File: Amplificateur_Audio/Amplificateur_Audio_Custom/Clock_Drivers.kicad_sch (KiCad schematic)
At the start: 59 parts, among them J301 Conn_02x10_Odd_Even, Q301 NMOS, Q302 NMOS, U301 74LVC1G125, U302 74LVC1G125, U303 74LVC1G125, U304 74LVC1G125, U305 74LVC1G125, U306 74LVC1G125, U307 74LVC1G125, U308 74LVC1G125, U309 74LVC1G125, U310 74LVC1G125

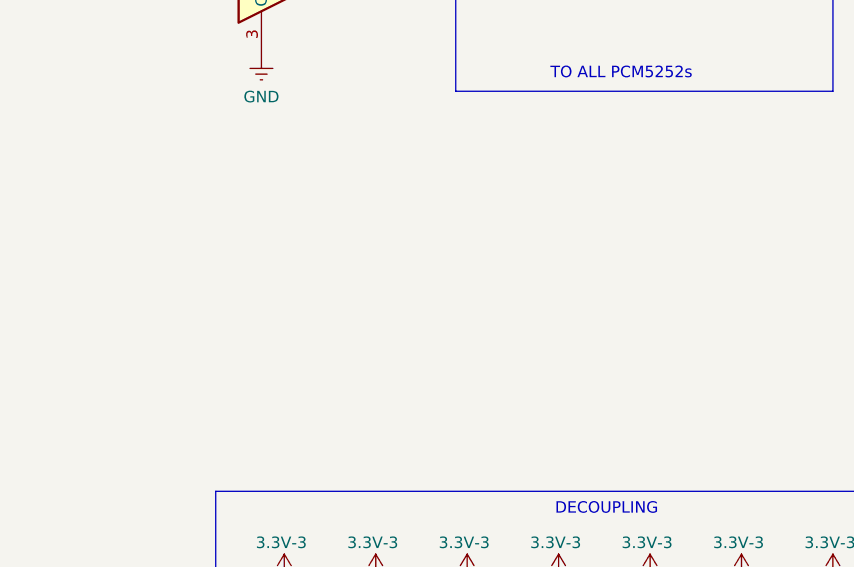
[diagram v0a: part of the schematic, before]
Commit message: Ajout de l'assignation des compostants et des empreintes jusqu'à la page 6
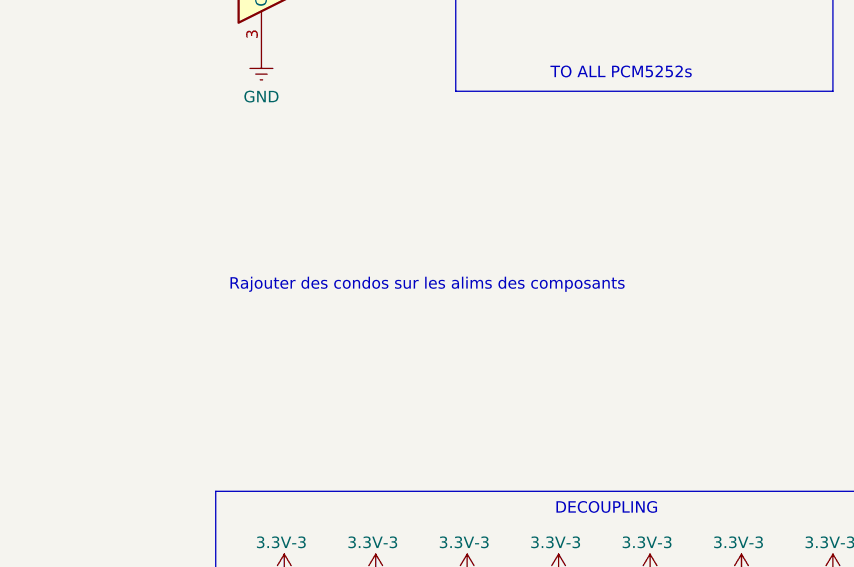
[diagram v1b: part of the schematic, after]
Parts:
- C301, C302, C303, C304, C305, C306, C307, C308: footprint (none) -> Capacitor_SMD:C_0402_1005Metric_Pad0.74x0.62mm_HandSolder
- D301, D302: footprint (none) -> LED_SMD:LED_0805_2012Metric_Pad1.15x1.40mm_HandSolder
- J301: footprint (none) -> Connector_IDC:IDC-Header_2x10_P2.54mm_Vertical_SMD
- Q301, Q302: footprint (none) -> Package_TO_SOT_SMD:SOT-23
- R301, R302, R303, R304, R305, R306, R307, R308, R309, R310, R311, R312, R313, R314, R315, R316, R317, R318: footprint (none) -> Resistor_SMD:R_0402_1005Metric_Pad0.72x0.64mm_HandSolder
- R319, R320, R321, R322, R323, R324, R325, R326, R327, R328, R329, R330, R331, R332, R333, R334: footprint (none) -> Resistor_SMD:R_0201_0603Metric_Pad0.64x0.40mm_HandSolder
- U301, U302, U303, U304, U305, U306, U307, U308, U309, U310: footprint (none) -> Package_TO_SOT_SMD:SOT-353_SC-70-5_Handsoldering
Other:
- note added: "Rajouter des condos sur les alims des composants"

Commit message: Ajout de point de test et début du routage
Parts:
- TP301, TP302: footprint (none) -> TestPoint:TestPoint_Pad_D1.5mm
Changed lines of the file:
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@@
 			)
 		)
-		(property "Footprint" ""
+		(property "Footprint" "TestPoint:TestPoint_Pad_D1.5mm"
 			(at 67.945 176.53 0)
 			(effects
@@
 			)
 		)
-		(property "Footprint" ""
+		(property "Footprint" "TestPoint:TestPoint_Pad_D1.5mm"
 			(at 67.945 115.57 0)
 			(effects

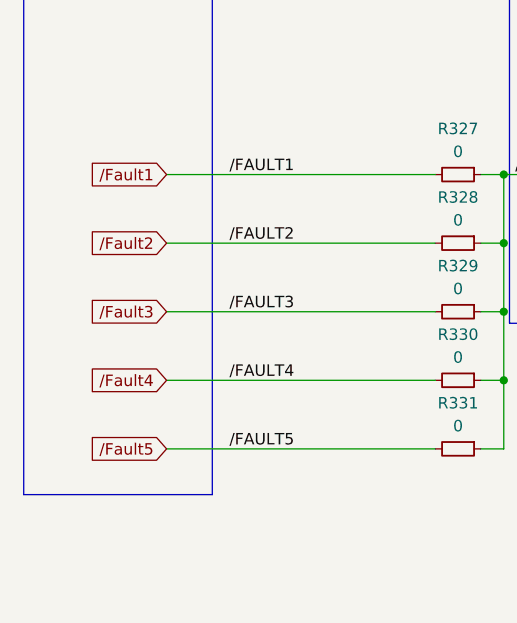
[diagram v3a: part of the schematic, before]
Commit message: Affinage du routage
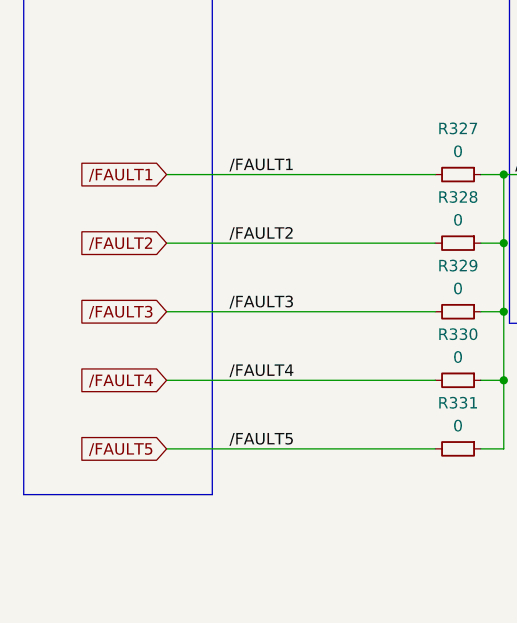
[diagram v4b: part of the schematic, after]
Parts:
- R301, R307, R313: footprint Resistor_SMD:R_0402_1005Metric_Pad0.72x0.64mm_HandSolder -> Resistor_SMD:R_0402_1005Metric
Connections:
- net /Fault1 renamed /FAULT1
- net /Fault2 renamed /FAULT2
- net /Fault3 renamed /FAULT3
- net /Fault4 renamed /FAULT4
- net /Fault5 renamed /FAULT5
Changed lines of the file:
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@@
 		)
 	)
-	(global_label "{slash}Fault3"
+	(global_label "{slash}FAULT3"
 		(shape input)
 		(at 30.48 191.77 180)
@@
 		)
 		(property "Intersheetrefs" "${INTERSHEET_REFS}"
-			(at 20.1773 191.77 0)
+			(at 19.4514 191.77 0)
 			(effects
 				(font
@@
 		)
 	)
-	(global_label "{slash}Fault5"
+	(global_label "{slash}FAULT5"
 		(shape input)
 		(at 30.48 207.01 180)
@@
 		)
 		(property "Intersheetrefs" "${INTERSHEET_REFS}"
-			(at 20.1773 207.01 0)
+			(at 19.4514 207.01 0)
 			(effects
 				(font
@@
 		)
 	)
-	(global_label "{slash}Fault4"
+	(global_label "{slash}FAULT4"
 		(shape input)
 		(at 30.48 199.39 180)
@@
 		)
 		(property "Intersheetrefs" "${INTERSHEET_REFS}"
-			(at 20.1773 199.39 0)
+			(at 19.4514 199.39 0)
 			(effects
 				(font
@@
 		)
 	)
-	(global_label "{slash}Fault1"
+	(global_label "{slash}FAULT1"
 		(shape input)
 		(at 30.48 176.53 180)
@@
 		)
 		(property "Intersheetrefs" "${INTERSHEET_REFS}"
-			(at 20.1773 176.53 0)
+			(at 19.4514 176.53 0)
 			(effects
 				(font
@@
 		)
 	)
-	(global_label "{slash}Fault2"
+	(global_label "{slash}FAULT2"
 		(shape input)
 		(at 30.48 184.15 180)
@@
 		)
 		(property "Intersheetrefs" "${INTERSHEET_REFS}"
-			(at 20.1773 184.15 0)
+			(at 19.4514 184.15 0)
 			(effects
 				(font
@@
 			)
 		)
-		(property "Footprint" "Resistor_SMD:R_0402_1005Metric_Pad0.72x0.64mm_HandSolder"
+		(property "Footprint" "Resistor_SMD:R_0402_1005Metric"
 			(at 359.41 113.03 0)
 			(effects
@@
 			)
 		)
-		(property "Footprint" "Resistor_SMD:R_0402_1005Metric_Pad0.72x0.64mm_HandSolder"
+		(property "Footprint" "Resistor_SMD:R_0402_1005Metric"
 			(at 359.41 179.07 0)
 			(effects
@@
 			)
 		)
-		(property "Footprint" "Resistor_SMD:R_0402_1005Metric_Pad0.72x0.64mm_HandSolder"
+		(property "Footprint" "Resistor_SMD:R_0402_1005Metric"
 			(at 359.41 46.99 0)
 			(effects

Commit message: Refactor : hierarchical template channels for multichannel routing
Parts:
- C301, C302, C303, C304, C305, C306, C307, C308: footprint Capacitor_SMD:C_0402_1005Metric_Pad0.74x0.62mm_HandSolder -> Capacitor_SMD:C_0402_1005Metric
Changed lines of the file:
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@@
 			)
 		)
-		(property "Footprint" "Capacitor_SMD:C_0402_1005Metric_Pad0.74x0.62mm_HandSolder"
+		(property "Footprint" "Capacitor_SMD:C_0402_1005Metric"
 			(at 201.93 219.71 0)
 			(effects
@@
 			)
 		)
-		(property "Footprint" "Capacitor_SMD:C_0402_1005Metric_Pad0.74x0.62mm_HandSolder"
+		(property "Footprint" "Capacitor_SMD:C_0402_1005Metric"
 			(at 242.57 219.71 0)
 			(effects
@@
 			)
 		)
-		(property "Footprint" "Capacitor_SMD:C_0402_1005Metric_Pad0.74x0.62mm_HandSolder"
+		(property "Footprint" "Capacitor_SMD:C_0402_1005Metric"
 			(at 262.89 219.71 0)
 			(effects
@@
 			)
 		)
-		(property "Footprint" "Capacitor_SMD:C_0402_1005Metric_Pad0.74x0.62mm_HandSolder"
+		(property "Footprint" "Capacitor_SMD:C_0402_1005Metric"
 			(at 212.09 219.71 0)
 			(effects
@@
 			)
 		)
-		(property "Footprint" "Capacitor_SMD:C_0402_1005Metric_Pad0.74x0.62mm_HandSolder"
+		(property "Footprint" "Capacitor_SMD:C_0402_1005Metric"
 			(at 252.73 219.71 0)
 			(effects
@@
 			)
 		)
-		(property "Footprint" "Capacitor_SMD:C_0402_1005Metric_Pad0.74x0.62mm_HandSolder"
+		(property "Footprint" "Capacitor_SMD:C_0402_1005Metric"
 			(at 222.25 219.71 0)
 			(effects
@@
 			)
 		)
-		(property "Footprint" "Capacitor_SMD:C_0402_1005Metric_Pad0.74x0.62mm_HandSolder"
+		(property "Footprint" "Capacitor_SMD:C_0402_1005Metric"
 			(at 232.41 219.71 0)
 			(effects
@@
 			)
 		)
-		(property "Footprint" "Capacitor_SMD:C_0402_1005Metric_Pad0.74x0.62mm_HandSolder"
+		(property "Footprint" "Capacitor_SMD:C_0402_1005Metric"
 			(at 273.05 219.71 0)
 			(effects
